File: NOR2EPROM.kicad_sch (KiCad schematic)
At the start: 7 parts, among them U1 SN74LVC245APW, U2 SN74LVC245APW, U3 MX29LV320, U4 27C322, U5 SN74LVC245APW, U6 SN74LVC245APW, U7 SN74LVC245APW

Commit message: finalize alpha schematic done
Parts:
- added U8: LD1117S33TR_SOT223, Package_TO_SOT_SMD:SOT-223-3_TabPin2, symbol Regulator_Linear:LD1117S33TR_SOT223
- U1, U2, U5: value SN74LVC245APW -> SN74LVC245
- U6, U7: value SN74LVC245APW -> SN74HCT245
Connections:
- net +3.3V: now also U1.20 (VCC), U2.20 (VCC), U5.20 (VCC), U8.2 (VO)
- net +5V: now also U6.20 (VCC), U7.20 (VCC), U8.3 (VI)
- net EPROM_A0: now also U1.18 (B1); no longer U1.2 (A1)
- net EPROM_A1: now also U1.17 (B2); no longer U1.3 (A2)
- net EPROM_A10: now also U2.16 (B3); no longer U2.4 (A3)
- net EPROM_A11: now also U2.15 (B4); no longer U2.5 (A4)
- net EPROM_A12: now also U2.14 (B5); no longer U2.6 (A5)
- net EPROM_A13: now also U2.13 (B6); no longer U2.7 (A6)
- net EPROM_A14: now also U2.12 (B7); no longer U2.8 (A7)
- net EPROM_A15: now also U2.11 (B8); no longer U2.9 (A8)
- net EPROM_A16: now also U5.18 (B1); no longer U5.2 (A1)
- net EPROM_A17: now also U5.17 (B2); no longer U5.3 (A2)
- net EPROM_A18: now also U5.16 (B3); no longer U5.4 (A3)
- net EPROM_A19: now also U5.15 (B4); no longer U5.5 (A4)
- net EPROM_A2: now also U1.16 (B3); no longer U1.4 (A3)
- net EPROM_A20: now also U5.14 (B5); no longer U5.6 (A5)
- net EPROM_A3: now also U1.15 (B4); no longer U1.5 (A4)
- net EPROM_A4: now also U1.14 (B5); no longer U1.6 (A5)
- net EPROM_A5: now also U1.13 (B6); no longer U1.7 (A6)
- net EPROM_A6: now also U1.12 (B7); no longer U1.8 (A7)
- net EPROM_A7: now also U1.11 (B8); no longer U1.9 (A8)
- net EPROM_A8: now also U2.18 (B1); no longer U2.2 (A1)
- net EPROM_A9: now also U2.17 (B2); no longer U2.3 (A2)
- net GND: now also U1.1 (DIR), U1.19 (~{OE}), U2.1 (DIR), U2.19 (~{OE}), U5.1 (DIR), U5.19 (~{OE}), U6.1 (DIR), U6.19 (~{OE}), U7.1 (DIR), U7.19 (~{OE}), U8.1 (GND)
- net NOR_A0: now also U1.2 (A1); no longer U1.18 (B1)
- net NOR_A1: now also U1.3 (A2); no longer U1.17 (B2)
- net NOR_A10: now also U2.4 (A3); no longer U2.16 (B3)
- net NOR_A11: now also U2.5 (A4); no longer U2.15 (B4)
- net NOR_A12: now also U2.6 (A5); no longer U2.14 (B5)
- net NOR_A13: now also U2.7 (A6); no longer U2.13 (B6)
- net NOR_A14: now also U2.8 (A7); no longer U2.12 (B7)
- net NOR_A15: now also U2.9 (A8); no longer U2.11 (B8)
- net NOR_A16: now also U5.2 (A1); no longer U5.18 (B1)
- net NOR_A17: now also U5.3 (A2); no longer U5.17 (B2)
- net NOR_A18: now also U5.4 (A3); no longer U5.16 (B3)
- net NOR_A19: now also U5.5 (A4); no longer U5.15 (B4)
- net NOR_A2: now also U1.4 (A3); no longer U1.16 (B3)
- net NOR_A20: now also U5.6 (A5); no longer U5.14 (B5)
- net NOR_A3: now also U1.5 (A4); no longer U1.15 (B4)
- net NOR_A4: now also U1.6 (A5); no longer U1.14 (B5)
- net NOR_A5: now also U1.7 (A6); no longer U1.13 (B6)
- net NOR_A6: now also U1.8 (A7); no longer U1.12 (B7)
- net NOR_A7: now also U1.9 (A8); no longer U1.11 (B8)
- net NOR_A8: now also U2.2 (A1); no longer U2.18 (B1)
- net NOR_A9: now also U2.3 (A2); no longer U2.17 (B2)
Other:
- moved on the sheet: U1, U2, U5, U6, U7

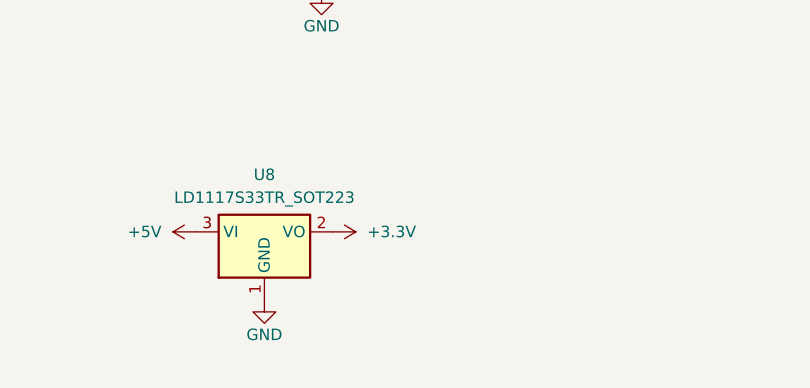
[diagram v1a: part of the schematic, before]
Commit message: add output cap, position components before routing
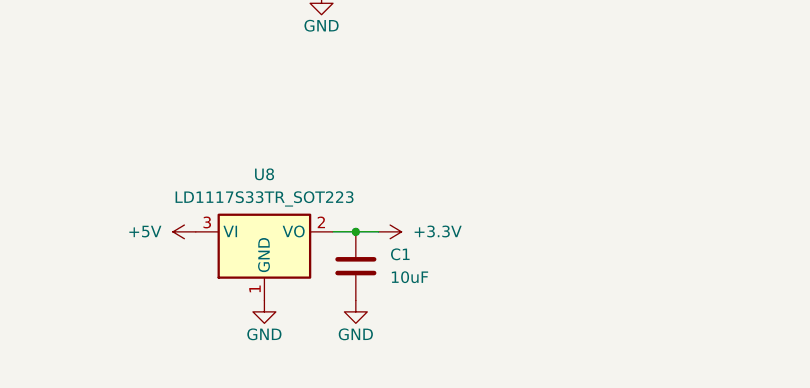
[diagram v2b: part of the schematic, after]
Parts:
- added C1: 10uF, Capacitor_SMD:C_0805_2012Metric, symbol Device:C
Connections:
- net +3.3V: now also C1.1
- net GND: now also C1.2
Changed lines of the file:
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@@
 	(paper "A4")
 	(junction
+		(at 146.05 171.45)
+		(diameter 0)
+		(color 0 0 0 0)
+	)
+	(junction
 		(at 60.96 181.61)
 		(diameter 0)
@@
 	(wire
 		(pts
+			(xy 143.51 171.45) (xy 146.05 171.45)
+		)
+		(stroke
+			(width 0)
+			(type default)
+		)
+	)
+	(wire
+		(pts
+			(xy 146.05 171.45) (xy 148.59 171.45)
+		)
+		(stroke
+			(width 0)
+			(type default)
+		)
+	)
+	(wire
+		(pts
 			(xy 58.42 181.61) (xy 60.96 181.61)
 		)
@@
 	)
 	(symbol
+		(lib_id "Device:C")
+		(at 146.05 175.26 0)
+		(unit 1)
+		(exclude_from_sim no)
+		(in_bom yes)
+		(on_board yes)
+		(dnp no)
+		(fields_autoplaced yes)
+		(property "Reference" "C1"
+			(at 149.86 173.9899 0)
+			(effects
+				(font
+					(size 1.27 1.27)
+				)
+				(justify left)
+			)
+		)
+		(property "Value" "10uF"
+			(at 149.86 176.5299 0)
+			(effects
+				(font
+					(size 1.27 1.27)
+				)
+				(justify left)
+			)
+		)
+		(property "Footprint" "Capacitor_SMD:C_0805_2012Metric"
+			(at 147.0152 179.07 0)
+			(effects
+				(font
+					(size 1.27 1.27)
+				)
+				(hide yes)
+			)
+		)
+		(property "Datasheet" "~"
+			(at 146.05 175.26 0)
+			(effects
+				(font
+					(size 1.27 1.27)
+				)
+				(hide yes)
+			)
+		)
+		(property "Description" "Unpolarized capacitor"
+			(at 146.05 175.26 0)
+			(effects
+				(font
+					(size 1.27 1.27)
+				)
+				(hide yes)
+			)
+		)
+		(pin "2"
+		)
+		(pin "1"
+		)
+		(instances
+			(project ""
+				(path "/fe8ca86c-10a4-4601-b9fb-6ff67a603b64"
+					(reference "C1")
+					(unit 1)
+				)
+			)
+		)
+	)
+	(symbol
 		(lib_id "power:GND")
 		(at 59.69 85.09 0)
@@
 	(symbol
 		(lib_id "power:+3.3V")
-		(at 143.51 171.45 270)
+		(at 148.59 171.45 270)
 		(unit 1)
 		(exclude_from_sim no)
@@
 		(fields_autoplaced yes)
 		(property "Reference" "#PWR027"
-			(at 139.7 171.45 0)
+			(at 144.78 171.45 0)
 			(effects
 				(font
@@
 		)
 		(property "Value" "+3.3V"
-			(at 147.32 171.4499 90)
+			(at 152.4 171.4499 90)
 			(effects
 				(font
@@
 		)
 		(property "Footprint" ""
-			(at 143.51 171.45 0)
+			(at 148.59 171.45 0)
 			(effects
 				(font
@@
 		)
 		(property "Datasheet" ""
-			(at 143.51 171.45 0)
+			(at 148.59 171.45 0)
 			(effects
 				(font
@@
 		)
 		(property "Description" "Power symbol creates a global label with name \"+3.3V\""
-			(at 143.51 171.45 0)
+			(at 148.59 171.45 0)
 			(effects
 				(font
@@
 					(unit 1)
 				)
+			)
+		)
+	)
+	(symbol
+		(lib_id "power:GND")
+		(at 146.05 179.07 0)
+		(unit 1)
+		(exclude_from_sim no)
+		(in_bom yes)
+		(on_board yes)
+		(dnp no)
+		(property "Reference" "#PWR029"
+			(at 146.05 185.42 0)
+			(effects
+				(font
+					(size 1.27 1.27)
+				)
+				(hide yes)
+			)
+		)
+		(property "Value" "GND"
+			(at 146.05 182.88 0)
+			(effects
+				(font
+					(size 1.27 1.27)
+				)
+			)
+		)
+		(property "Footprint" ""
+			(at 146.05 179.07 0)
+			(effects
+				(font
+					(size 1.27 1.27)
+				)
+				(hide yes)
+			)
+		)
+		(property "Datasheet" ""
+			(at 146.05 179.07 0)
+			(effects
+				(font
+					(size 1.27 1.27)
+				)
+				(hide yes)
+			)
+		)
+		(property "Description" "Power symbol creates a global label with name \"GND\" , ground"
+			(at 146.05 179.07 0)
+			(effects
+				(font
+					(size 1.27 1.27)
+				)
+				(hide yes)
+			)
+		)
+		(pin "1"
+		)
+		(instances
+			(project "NOR2EPROM"
+				(path "/fe8ca86c-10a4-4601-b9fb-6ff67a603b64"
+					(reference "#PWR029")
+					(unit 1)
+				)

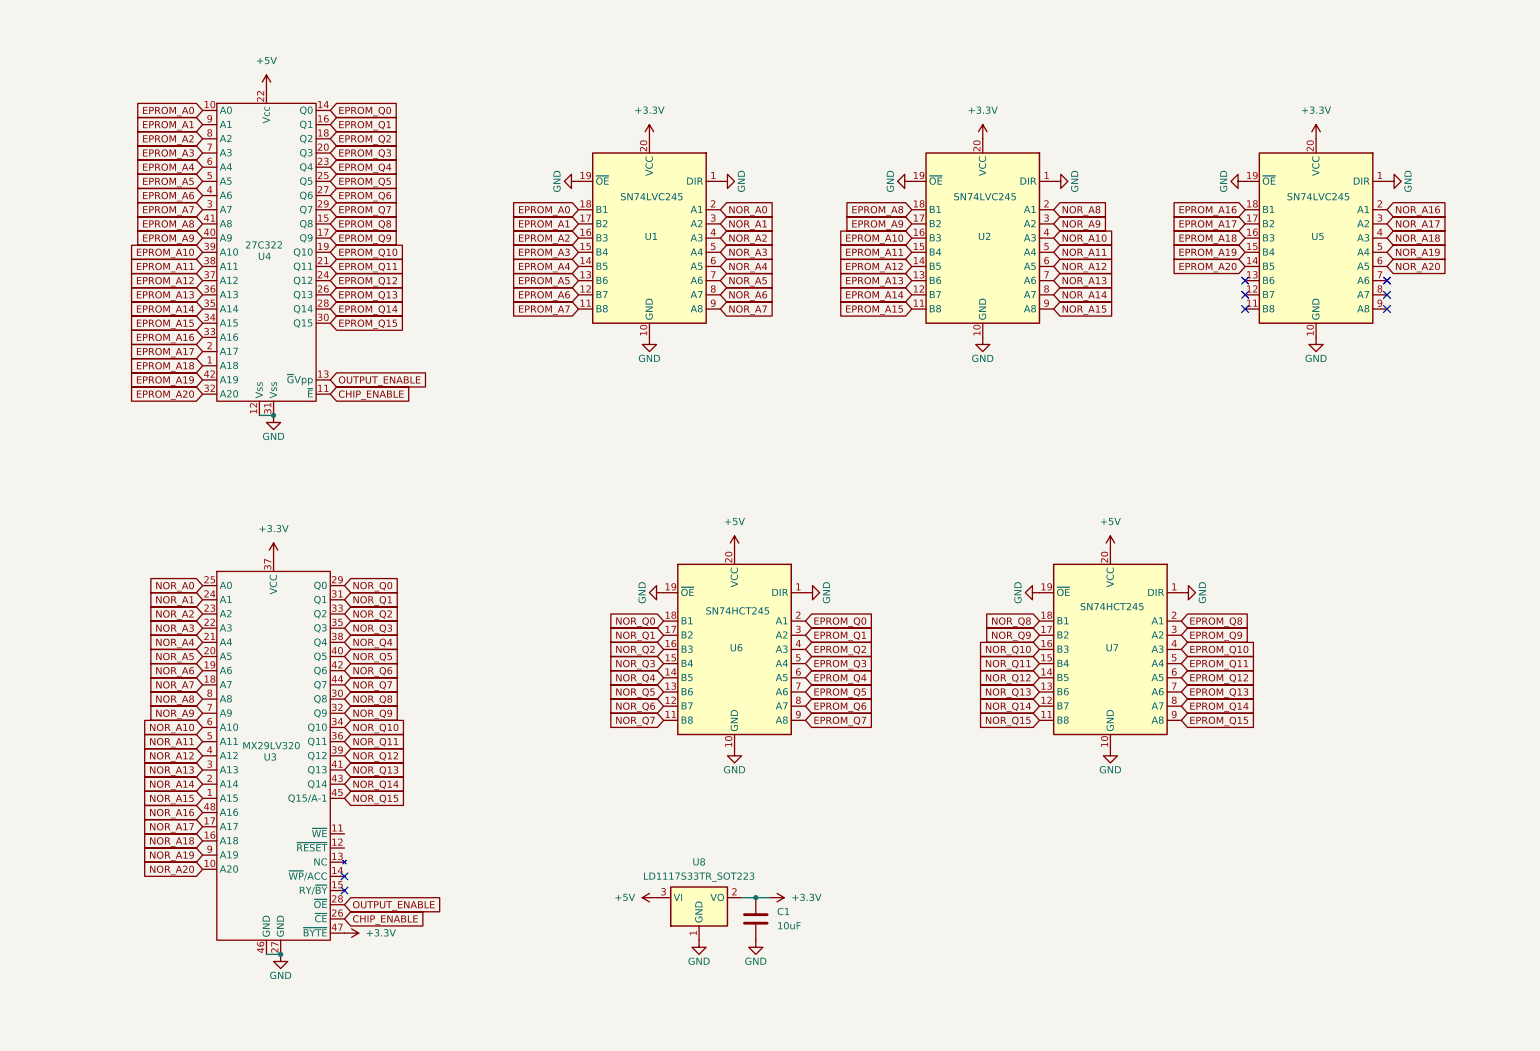
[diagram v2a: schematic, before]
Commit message: clean up schematic
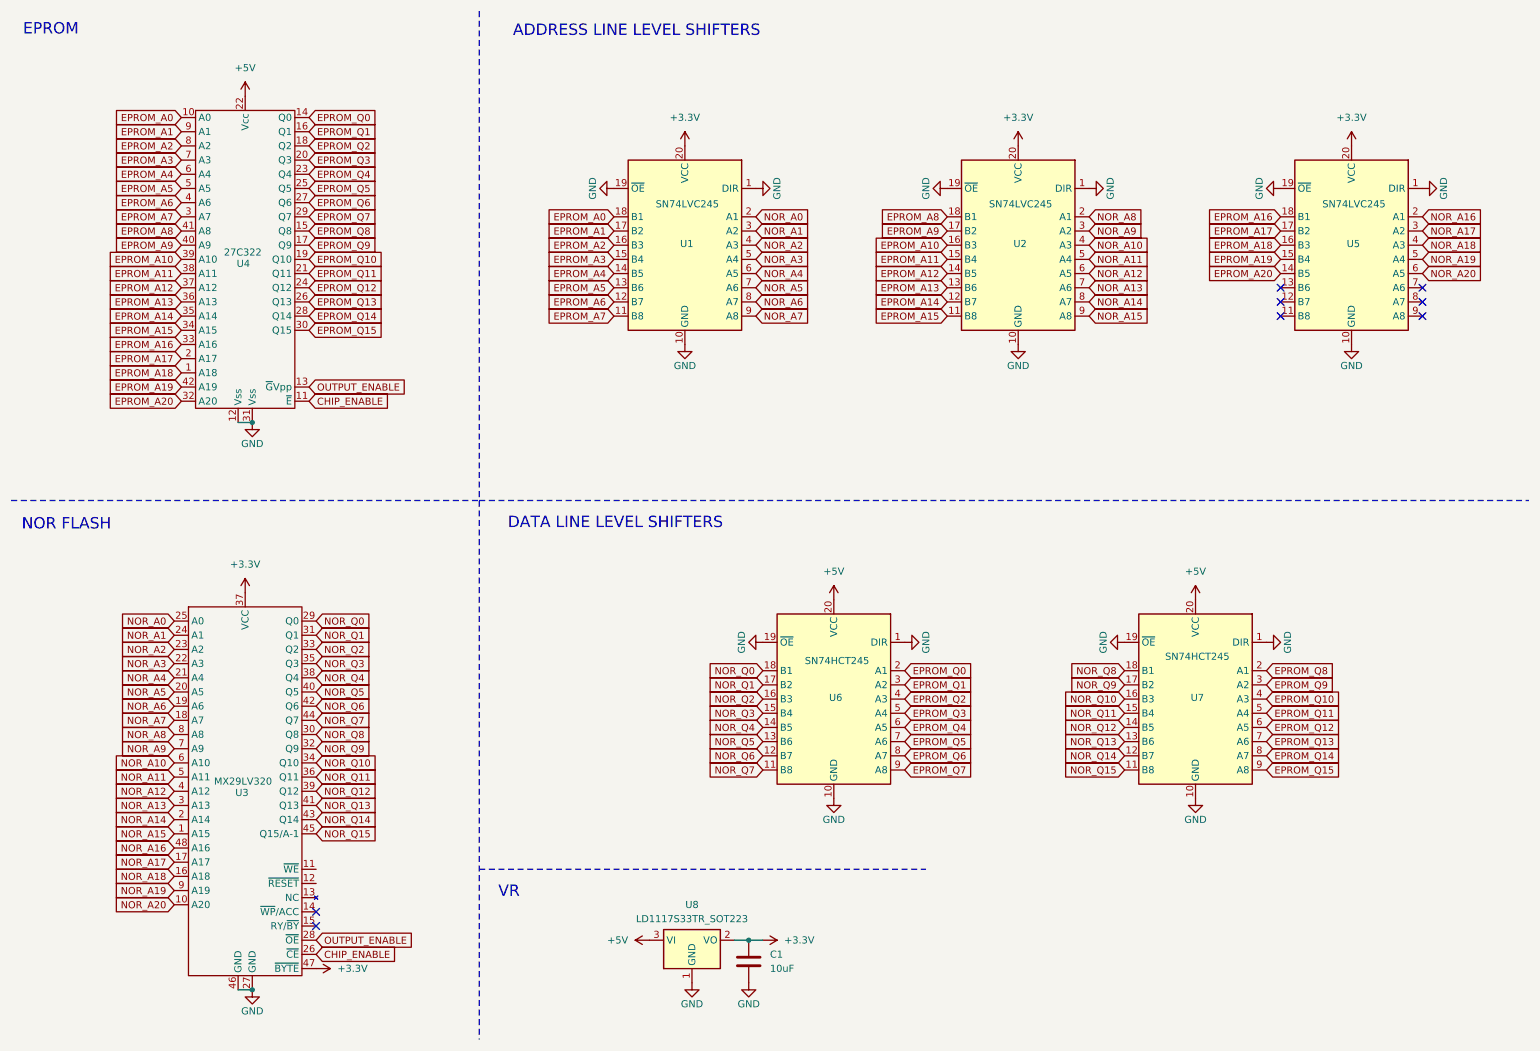
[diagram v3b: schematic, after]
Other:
- note added: "ADDRESS LINE LEVEL SHIFTERS"
- note added: "DATA LINE LEVEL SHIFTERS"
- note added: "EPROM"
- note added: "NOR FLASH"
- note added: "VR"
- moved on the sheet: C1, U1, U2, U3, U4, U5, U6, U7, U8

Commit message: level shift OE and CE lines
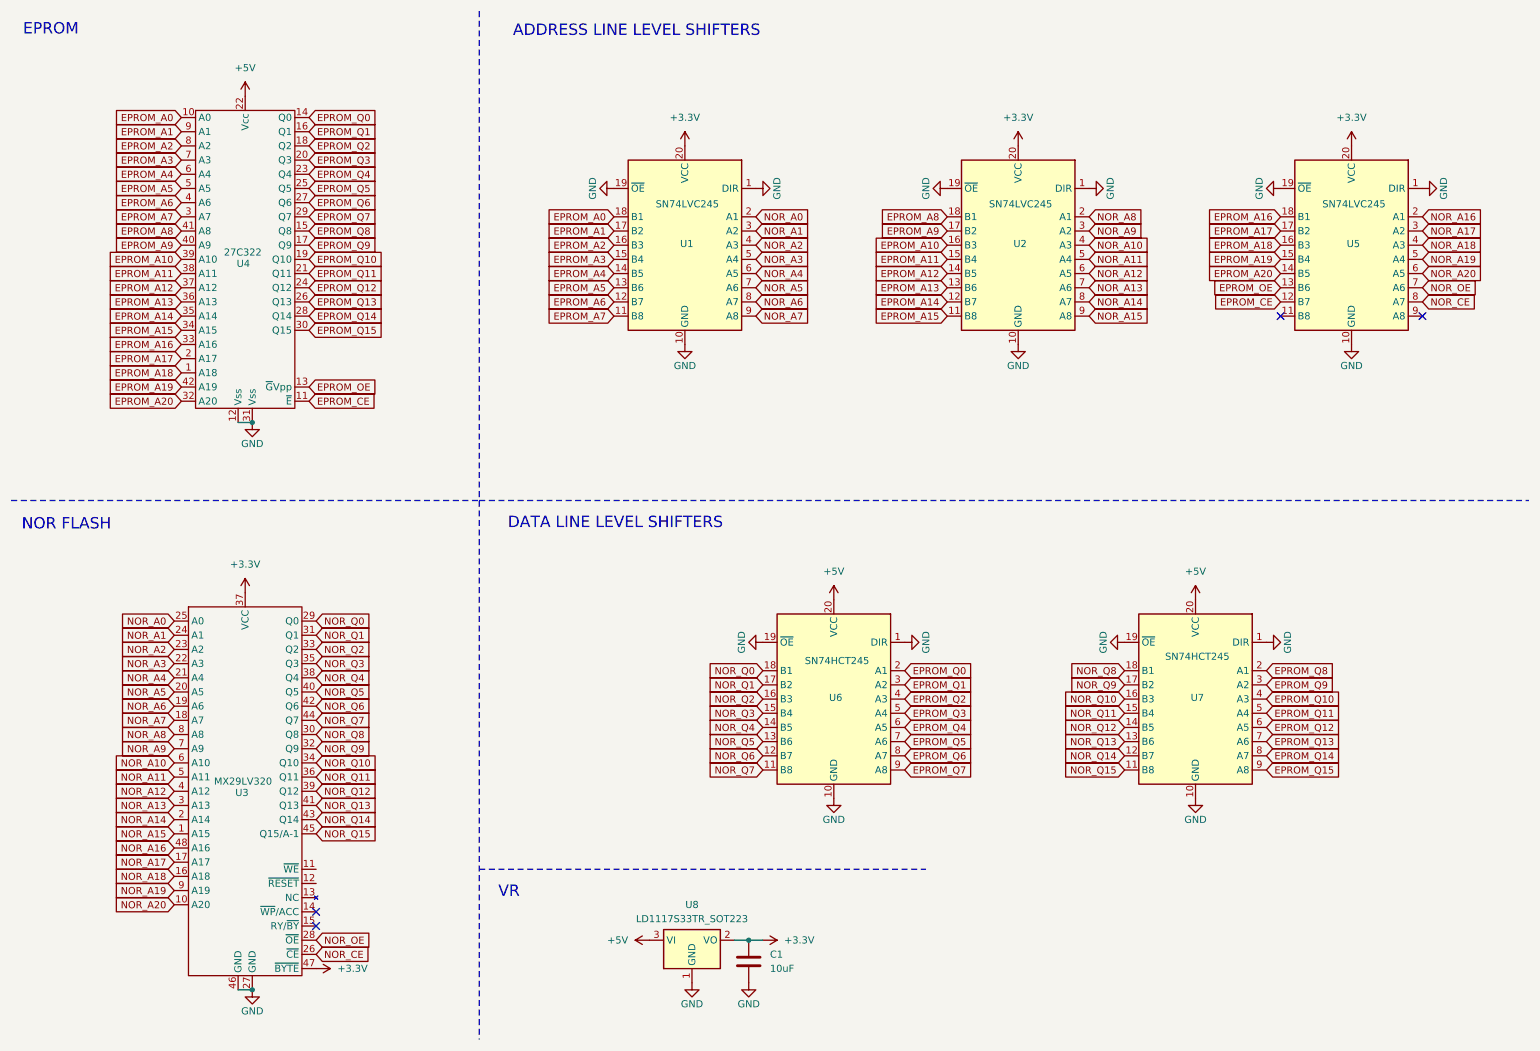
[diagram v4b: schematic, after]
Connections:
- net EPROM_CE: now reaches U5.12 (B7)
- net EPROM_CE: now also U4.11 (~{E})
- net EPROM_OE: now reaches U5.13 (B6)
- net EPROM_OE: now also U4.13 (~{G}Vpp)
- net NOR_OE: now reaches U5.7 (A6)
- net NOR_OE: now also U3.28 (~{OE})
- net NOR_CE: now reaches U5.8 (A7)
- net NOR_CE: now also U3.26 (~{CE})
- removed net CHIP_ENABLE: U3.26 (~{CE}), U4.11 (~{E})
- removed net OUTPUT_ENABLE: U3.28 (~{OE}), U4.13 (~{G}Vpp)
- no-connect marks 8 -> 4
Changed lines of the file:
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@@
 	)
 	(no_connect
-		(at 240.03 62.23)
-	)
-	(no_connect
 		(at 67.31 176.53)
 	)
 	(no_connect
-		(at 240.03 64.77)
-	)
-	(no_connect
-		(at 265.43 62.23)
-	)
-	(no_connect
 		(at 240.03 67.31)
 	)
 	(no_connect
-		(at 265.43 64.77)
-	)
-	(no_connect
 		(at 265.43 67.31)
 	)
@@
 		)
 	)
-	(global_label "CHIP_ENABLE"
+	(global_label "EPROM_CE"
 		(shape input)
 		(at 66.04 82.55 0)
@@
 		)
 		(property "Intersheetrefs" "${INTERSHEET_REFS}"
-			(at 81.4833 82.55 0)
+			(at 78.8827 82.55 0)
 			(effects
 				(font
@@
 		)
 	)
-	(global_label "OUTPUT_ENABLE"
+	(global_label "EPROM_OE"
 		(shape input)
 		(at 66.04 80.01 0)
@@
 		)
 		(property "Intersheetrefs" "${INTERSHEET_REFS}"
-			(at 84.2047 80.01 0)
+			(at 78.9432 80.01 0)
 			(effects
 				(font
@@
 		)
 	)
+	(global_label "EPROM_CE"
+		(shape input)
+		(at 240.03 64.77 180)
+		(fields_autoplaced yes)
+		(effects
+			(font
+				(size 1.27 1.27)
+			)
+			(justify right)
+		)
+		(property "Intersheetrefs" "${INTERSHEET_REFS}"
+			(at 227.1873 64.77 0)
+			(effects
+				(font
+					(size 1.27 1.27)
+				)
+				(justify right)
+				(hide yes)
+			)
+		)
+	)
 	(global_label "EPROM_A9"
 		(shape input)
@@
 		)
 	)
+	(global_label "NOR_CE"
+		(shape input)
+		(at 265.43 64.77 0)
+		(fields_autoplaced yes)
+		(effects
+			(font
+				(size 1.27 1.27)
+			)
+			(justify left)
+		)
+		(property "Intersheetrefs" "${INTERSHEET_REFS}"
+			(at 275.7328 64.77 0)
+			(effects
+				(font
+					(size 1.27 1.27)
+				)
+				(justify left)
+				(hide yes)
+			)
+		)
+	)
 	(global_label "NOR_A13"
 		(shape input)
@@
 		)
 	)
+	(global_label "NOR_OE"
+		(shape input)
+		(at 265.43 62.23 0)
+		(fields_autoplaced yes)
+		(effects
+			(font
+				(size 1.27 1.27)
+			)
+			(justify left)
+		)
+		(property "Intersheetrefs" "${INTERSHEET_REFS}"
+			(at 275.7933 62.23 0)
+			(effects
+				(font
+					(size 1.27 1.27)
+				)
+				(justify left)
+				(hide yes)
+			)
+		)
+	)
 	(global_label "NOR_A1"
 		(shape input)
@@
 		)
 	)
+	(global_label "EPROM_OE"
+		(shape input)
+		(at 240.03 62.23 180)
+		(fields_autoplaced yes)
+		(effects
+			(font
+				(size 1.27 1.27)
+			)
+			(justify right)
+		)
+		(property "Intersheetrefs" "${INTERSHEET_REFS}"
+			(at 227.1268 62.23 0)
+			(effects
+				(font
+					(size 1.27 1.27)
+				)
+				(justify right)
+				(hide yes)
+			)
+		)
+	)
 	(global_label "EPROM_A8"
 		(shape input)
@@
 		)
 	)
-	(global_label "CHIP_ENABLE"
+	(global_label "NOR_CE"
 		(shape input)
 		(at 67.31 181.61 0)
@@
 		)
 		(property "Intersheetrefs" "${INTERSHEET_REFS}"
-			(at 82.7533 181.61 0)
+			(at 77.6128 181.61 0)
 			(effects
 				(font
@@
 		)
 	)
-	(global_label "OUTPUT_ENABLE"
+	(global_label "NOR_OE"
 		(shape input)
 		(at 67.31 179.07 0)
@@
 		)
 		(property "Intersheetrefs" "${INTERSHEET_REFS}"
-			(at 85.4747 179.07 0)
+			(at 77.6733 179.07 0)
 			(effects
 				(font
